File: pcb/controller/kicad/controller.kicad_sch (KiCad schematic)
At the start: 0 parts

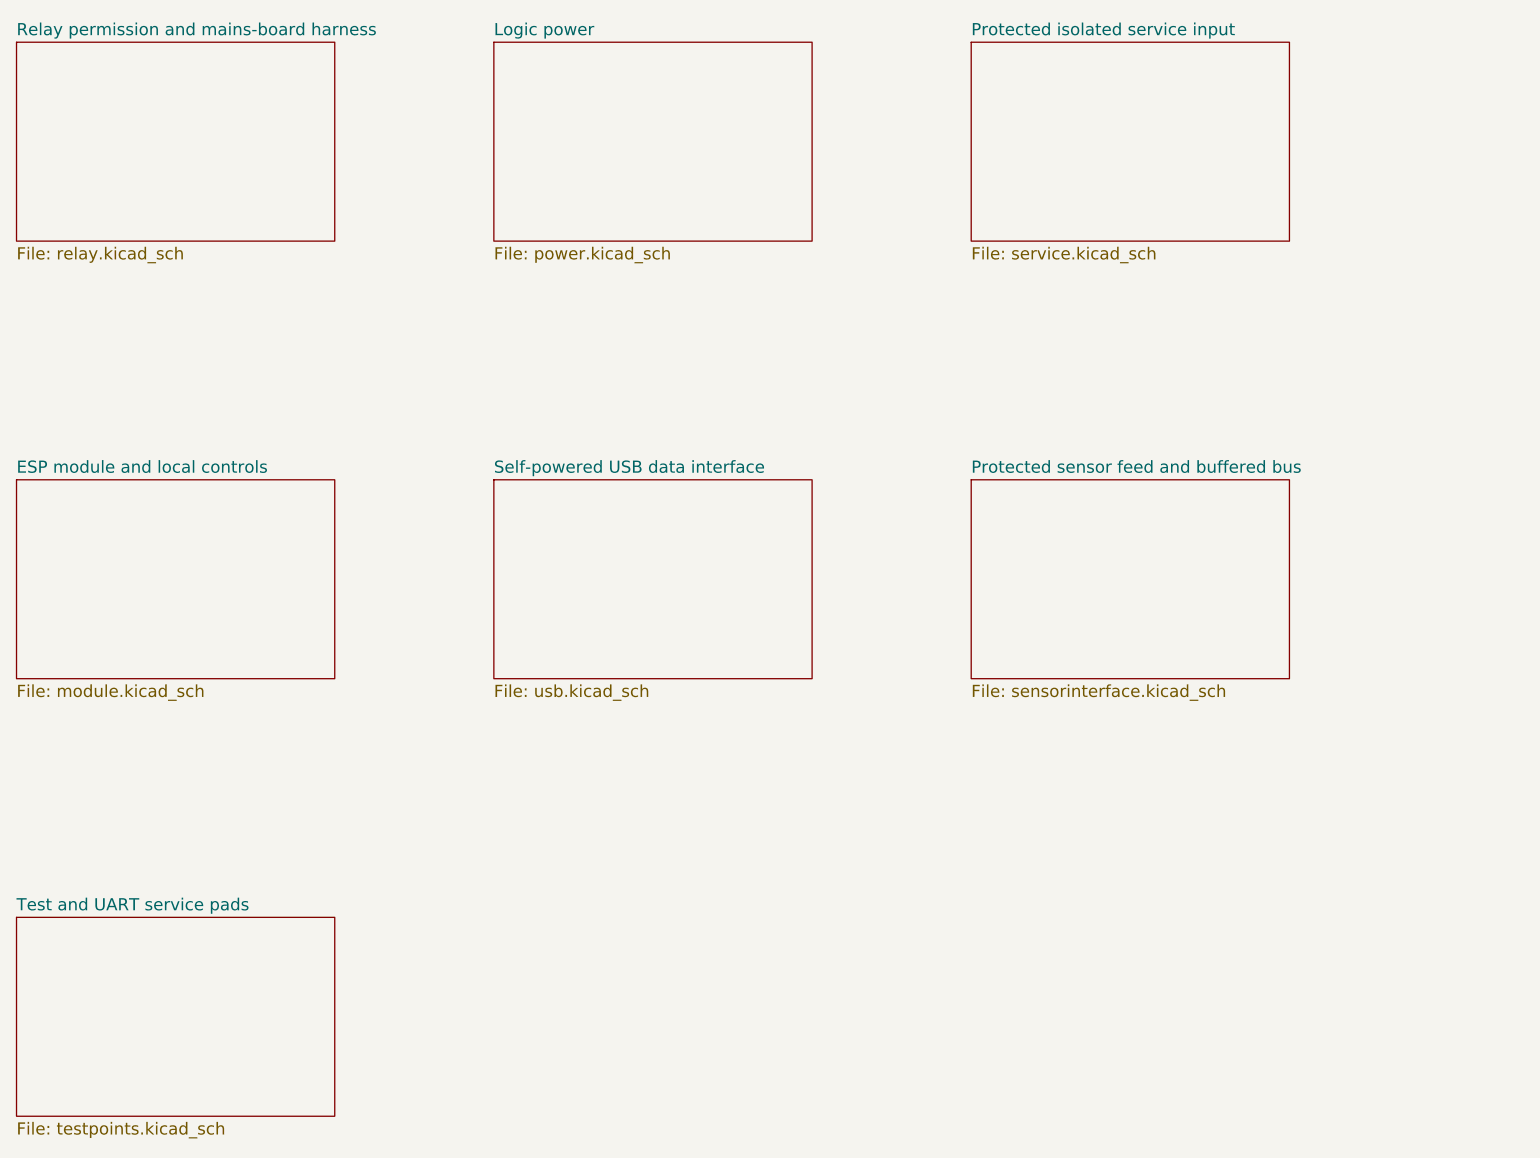
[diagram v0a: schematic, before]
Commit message: Prepare simplified shared-power boards for routing
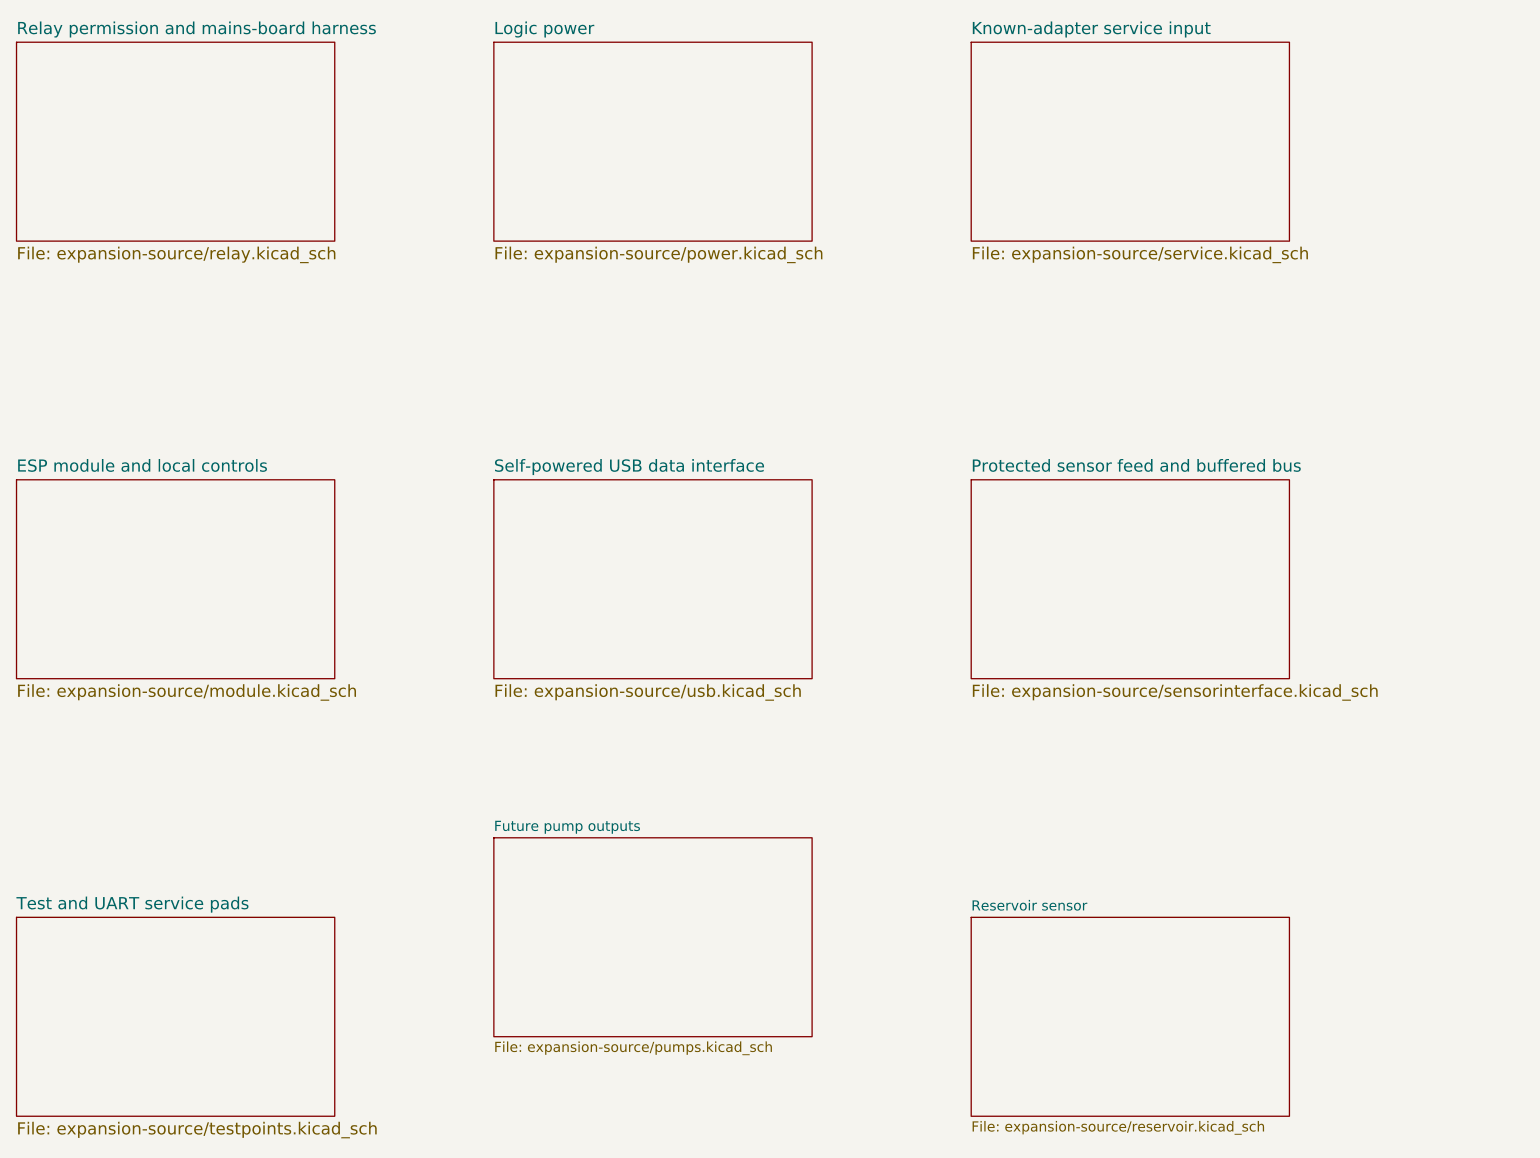
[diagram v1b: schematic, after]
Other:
- sheet Protected isolated service input renamed Known-adapter service input
- added sheet Future pump outputs (expansion-source/pumps.kicad_sch)
- added sheet Reservoir sensor (expansion-source/reservoir.kicad_sch)
- sheet ESP module and local controls: file module.kicad_sch -> expansion-source/module.kicad_sch
- sheet Known-adapter service input: file service.kicad_sch -> expansion-source/service.kicad_sch
- sheet Logic power: file power.kicad_sch -> expansion-source/power.kicad_sch
- sheet Protected sensor feed and buffered bus: file sensorinterface.kicad_sch -> expansion-source/sensorinterface.kicad_sch
- sheet Relay permission and mains-board harness: file relay.kicad_sch -> expansion-source/relay.kicad_sch
- sheet Self-powered USB data interface: file usb.kicad_sch -> expansion-source/usb.kicad_sch
- sheet Test and UART service pads: file testpoints.kicad_sch -> expansion-source/testpoints.kicad_sch
